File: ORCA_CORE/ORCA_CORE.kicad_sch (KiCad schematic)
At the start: 0 parts

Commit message: making usp
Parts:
- added J1: Conn_01x03, symbol Connector_Generic:Conn_01x03
- added J2: Conn_01x04, symbol Connector_Generic:Conn_01x04
- added J3, J5, J6, J7: Conn_01x02, symbol Connector_Generic:Conn_01x02
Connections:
- net power/Vout_usp: now also J7.2 (Pin_2)
- net power/emerg_detector: now also J1.1 (Pin_1)
- net power/emerge_order: now also J1.3 (Pin_3)
- new net GND: J2.2 (Pin_2), J3.1 (Pin_1), J5.1 (Pin_1), J6.1 (Pin_1), J7.1 (Pin_1)
- new net power/5V_I2C: J2.1 (Pin_1)
- new net power/SCL_3V3: J2.3 (Pin_3)
- new net power/SDA_3V3: J2.4 (Pin_4)
- new net power/Vin_bat: J5.2 (Pin_2)
- new net power/Vin_ex: J6.2 (Pin_2)
- new net power/Vout_motor: J3.2 (Pin_2)
- new net power/power_checker: J1.2 (Pin_2)
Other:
- sheet power ports: added 5V_I2C, GND, SCL_3V3, SDA_3V3, Vin_bat, Vin_ex, Vout_motor, power_checker; removed GND_out, Vout_cpu, battery_checker

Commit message: made usp (sketch only)
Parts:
- added J8: Vin_power2usp, symbol Connector_Generic:Conn_01x02
- added J9: +5Vout_cpu, symbol Connector_Generic:Conn_01x02
- J1: value Conn_01x03 -> data_line_power
- J2: value Conn_01x04 -> I2C_power
- J3: value Conn_01x02 -> Vout_motor
- J5: value Conn_01x02 -> Vin_batt
- J6: value Conn_01x02 -> Vin_ex
- J7: value Conn_01x02 -> Vout_power2usp
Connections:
- net GND: now also J8.1 (Pin_1), J9.1 (Pin_1)
- net power/5V_I2C renamed power/3V_I2C
- new net usp/Vin: J8.2 (Pin_2)
- new net usp/Vout: J9.2 (Pin_2)
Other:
- sheet power ports: added 3V_I2C; removed 5V_I2C
- sheet usp ports: added GND, Vin, Vout; removed none
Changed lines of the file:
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@@
+    (stroke (width 0) (type default))
+  )
+  (wire (pts (xy 58.42 100.33) (xy 67.31 100.33))
     (stroke (width 0) (type default))
   )
@@
     (stroke (width 0) (type default))
   )
+  (wire (pts (xy 66.04 93.98) (xy 66.04 86.36))
+    (stroke (width 0) (type default))
+  )
+  (wire (pts (xy 58.42 93.98) (xy 66.04 93.98))
+    (stroke (width 0) (type default))
+  )
   (wire (pts (xy 71.12 53.34) (xy 80.01 53.34))
     (stroke (width 0) (type default))
@@
     (stroke (width 0) (type default))
   )
+  (symbol (lib_id "power:GND") (at 67.31 97.79 270) (unit 1)
+    (in_bom yes) (on_board yes) (dnp no) (fields_autoplaced)
+    (property "Reference" "#PWR069" (at 60.96 97.79 0)
+      (effects (font (size 1.27 1.27)) hide)
+    )
+    (property "Value" "GND" (at 63.5 97.79 90)
+      (effects (font (size 1.27 1.27)) (justify right))
+    )
+    (property "Footprint" "" (at 67.31 97.79 0)
+      (effects (font (size 1.27 1.27)) hide)
+    )
+    (property "Datasheet" "" (at 67.31 97.79 0)
+      (effects (font (size 1.27 1.27)) hide)
+    )
+    (pin "1")
+    (instances
+      (project "ORCA_CORE"
+        (path "/895d6bb7-4008-488b-a34b-0077e9f7e4a1"
+          (reference "#PWR069") (unit 1)
+        )
+      )
+    )
+  )
+  (symbol (lib_id "power:GND") (at 58.42 105.41 90) (unit 1)
+    (in_bom yes) (on_board yes) (dnp no) (fields_autoplaced)
+    (property "Reference" "#PWR070" (at 64.77 105.41 0)
+      (effects (font (size 1.27 1.27)) hide)
+    )
+    (property "Value" "GND" (at 62.23 105.41 90)
+      (effects (font (size 1.27 1.27)) (justify right))
+    )
+    (property "Footprint" "" (at 58.42 105.41 0)
+      (effects (font (size 1.27 1.27)) hide)
+    )
+    (property "Datasheet" "" (at 58.42 105.41 0)
+      (effects (font (size 1.27 1.27)) hide)
+    )
+    (pin "1")
+    (instances
+      (project "ORCA_CORE"
+        (path "/895d6bb7-4008-488b-a34b-0077e9f7e4a1"
+          (reference "#PWR070") (unit 1)
+        )
+      )
+    )
+  )
   (symbol (lib_id "power:GND") (at 27.94 29.21 90) (unit 1)
     (in_bom yes) (on_board yes) (dnp no) (fields_autoplaced)
@@
     )
   )
+  (symbol (lib_id "Connector_Generic:Conn_01x02") (at 72.39 97.79 0) (unit 1)
+    (in_bom yes) (on_board yes) (dnp no) (fields_autoplaced)
+    (property "Reference" "J9" (at 74.93 97.79 0)
+      (effects (font (size 1.27 1.27)) (justify left))
+    )
+    (property "Value" "+5Vout_cpu" (at 74.93 100.33 0)
+      (effects (font (size 1.27 1.27)) (justify left))
+    )
+    (property "Footprint" "" (at 72.39 97.79 0)
+      (effects (font (size 1.27 1.27)) hide)
+    )
+    (property "Datasheet" "~" (at 72.39 97.79 0)
+      (effects (font (size 1.27 1.27)) hide)
+    )
+    (pin "2")
+    (pin "1")
+    (instances
+      (project "ORCA_CORE"
+        (path "/895d6bb7-4008-488b-a34b-0077e9f7e4a1"
+          (reference "J9") (unit 1)
+        )
+      )
+    )
+  )
+  (symbol (lib_id "Connector_Generic:Conn_01x02") (at 63.5 81.28 90) (unit 1)
+    (in_bom yes) (on_board yes) (dnp no) (fields_autoplaced)
+    (property "Reference" "J8" (at 68.58 80.01 90)
+      (effects (font (size 1.27 1.27)) (justify right))
+    )
+    (property "Value" "Vin_power2usp" (at 68.58 82.55 90)
+      (effects (font (size 1.27 1.27)) (justify right))
+    )
+    (property "Footprint" "" (at 63.5 81.28 0)
+      (effects (font (size 1.27 1.27)) hide)
+    )
+    (property "Datasheet" "~" (at 63.5 81.28 0)
+      (effects (font (size 1.27 1.27)) hide)
+    )
+    (pin "2")
+    (pin "1")
+    (instances
+      (project "ORCA_CORE"
+        (path "/895d6bb7-4008-488b-a34b-0077e9f7e4a1"
+          (reference "J8") (unit 1)
+        )
+      )
+    )
+  )
   (symbol (lib_id "power:GND") (at 68.58 69.85 90) (unit 1)
     (in_bom yes) (on_board yes) (dnp no) (fields_autoplaced)
@@
       (effects (font (size 1.27 1.27)) (justify left))
     )
-    (property "Value" "Conn_01x04" (at 87.63 50.8 0)
+    (property "Value" "I2C_power" (at 87.63 50.8 0)
       (effects (font (size 1.27 1.27)) (justify left))
     )
@@
       (effects (font (size 1.27 1.27)) (justify left))
     )
-    (property "Value" "Conn_01x03" (at 87.63 38.1 0)
+    (property "Value" "data_line_power" (at 87.63 38.1 0)
       (effects (font (size 1.27 1.27)) (justify left))
     )
@@
     )
   )
+  (symbol (lib_id "power:GND") (at 63.5 86.36 0) (unit 1)
+    (in_bom yes) (on_board yes) (dnp no) (fields_autoplaced)
+    (property "Reference" "#PWR068" (at 63.5 92.71 0)
+      (effects (font (size 1.27 1.27)) hide)
+    )
+    (property "Value" "GND" (at 63.5 91.44 0)
+      (effects (font (size 1.27 1.27)))
+    )
+    (property "Footprint" "" (at 63.5 86.36 0)
+      (effects (font (size 1.27 1.27)) hide)
+    )
+    (property "Datasheet" "" (at 63.5 86.36 0)
+      (effects (font (size 1.27 1.27)) hide)
+    )
+    (pin "1")
+    (instances
+      (project "ORCA_CORE"
+        (path "/895d6bb7-4008-488b-a34b-0077e9f7e4a1"
+          (reference "#PWR068") (unit 1)
+        )
+      )
+    )
+  )
   (symbol (lib_id "power:GND") (at 27.94 43.18 90) (unit 1)
     (in_bom yes) (on_board yes) (dnp no) (fields_autoplaced)
@@
       (effects (font (size 1.27 1.27)) (justify left))
     )
-    (property "Value" "Conn_01x02" (at 68.58 77.47 90)
+    (property "Value" "Vout_power2usp" (at 68.58 77.47 90)
       (effects (font (size 1.27 1.27)) (justify left))
     )
@@
       (effects (font (size 1.27 1.27)))
     )
-    (property "Value" "Conn_01x02" (at 22.86 36.83 0)
+    (property "Value" "Vin_ex" (at 22.86 36.83 0)
       (effects (font (size 1.27 1.27)))
     )
@@
       (effects (font (size 1.27 1.27)))
     )
-    (property "Value" "Conn_01x02" (at 22.86 22.86 0)
+    (property "Value" "Vin_batt" (at 22.86 22.86 0)
       (effects (font (size 1.27 1.27)))
     )
@@
       (effects (font (size 1.27 1.27)) (justify left))
     )
-    (property "Value" "Conn_01x02" (at 87.63 26.67 0)
+    (property "Value" "Vout_motor" (at 87.63 26.67 0)
       (effects (font (size 1.27 1.27)) (justify left))
     )
@@
       (effects (font (size 1.27 1.27)) (justify right))
     )
-    (pin "5V_I2C" output (at 71.12 45.72 0)
-      (effects (font (size 1.27 1.27)) (justify right))
-    )
     (pin "GND" output (at 68.58 66.04 270)
       (effects (font (size 1.27 1.27)) (justify left))
     )
+    (pin "3V_I2C" output (at 71.12 45.72 0)
+      (effects (font (size 1.27 1.27)) (justify right))
+    )
     (instances
       (project "ORCA_CORE"
@@
     )
   )
-  (sheet (at 46.228 137.922) (size 32.131 24.765) (fields_autoplaced)
+  (sheet (at 45.72 90.932) (size 12.7 18.288) (fields_autoplaced)
     (stroke (width 0.1524) (type solid))
     (fill (color 255 255 255 0.0000))
-    (property "Sheetname" "usp" (at 46.228 137.2104 0)
+    (property "Sheetname" "usp" (at 45.72 90.2204 0)
       (effects (font (size 1.27 1.27)) (justify left bottom))
     )
-    (property "Sheetfile" "usp.kicad_sch" (at 46.228 163.2716 0)
+    (property "Sheetfile" "usp.kicad_sch" (at 45.72 109.8046 0)
       (effects (font (size 1.27 1.27)) (justify left top))
     )
+    (pin "GND" output (at 58.42 105.41 0)
+      (effects (font (size 1.27 1.27)) (justify right))
+    )
+    (pin "Vin" input (at 58.42 93.98 0)
+      (effects (font (size 1.27 1.27)) (justify right))
+    )
+    (pin "Vout" input (at 58.42 100.33 0)
+      (effects (font (size 1.27 1.27)) (justify right))
+    )
     (instances
       (project "ORCA_CORE"
@@
     )
   )
-  (sheet (at 107.188 57.277) (size 33.782 42.164) (fields_autoplaced)
+  (sheet (at 116.078 24.257) (size 33.782 42.164) (fields_autoplaced)
     (stroke (width 0.1524) (type solid))
     (fill (color 255 255 255 0.0000))
-    (property "Sheetname" "cpu" (at 107.188 56.5654 0)
+    (property "Sheetname" "cpu" (at 116.078 23.5454 0)
       (effects (font (size 1.27 1.27)) (justify left bottom))
     )
-    (property "Sheetfile" "cpu.kicad_sch" (at 107.188 100.0256 0)
+    (property "Sheetfile" "cpu.kicad_sch" (at 116.078 67.0056 0)
       (effects (font (size 1.27 1.27)) (justify left top))
     )
-    (property "フィールド2" "" (at 107.188 57.277 0)
-      (effects (font (size 1.27 1.27)) hide)
-    )
+    (property "フィールド2" "" (at 116.078 24.257 0)
+      (effects (font (size 1.27 1.27)) hide)
+    )

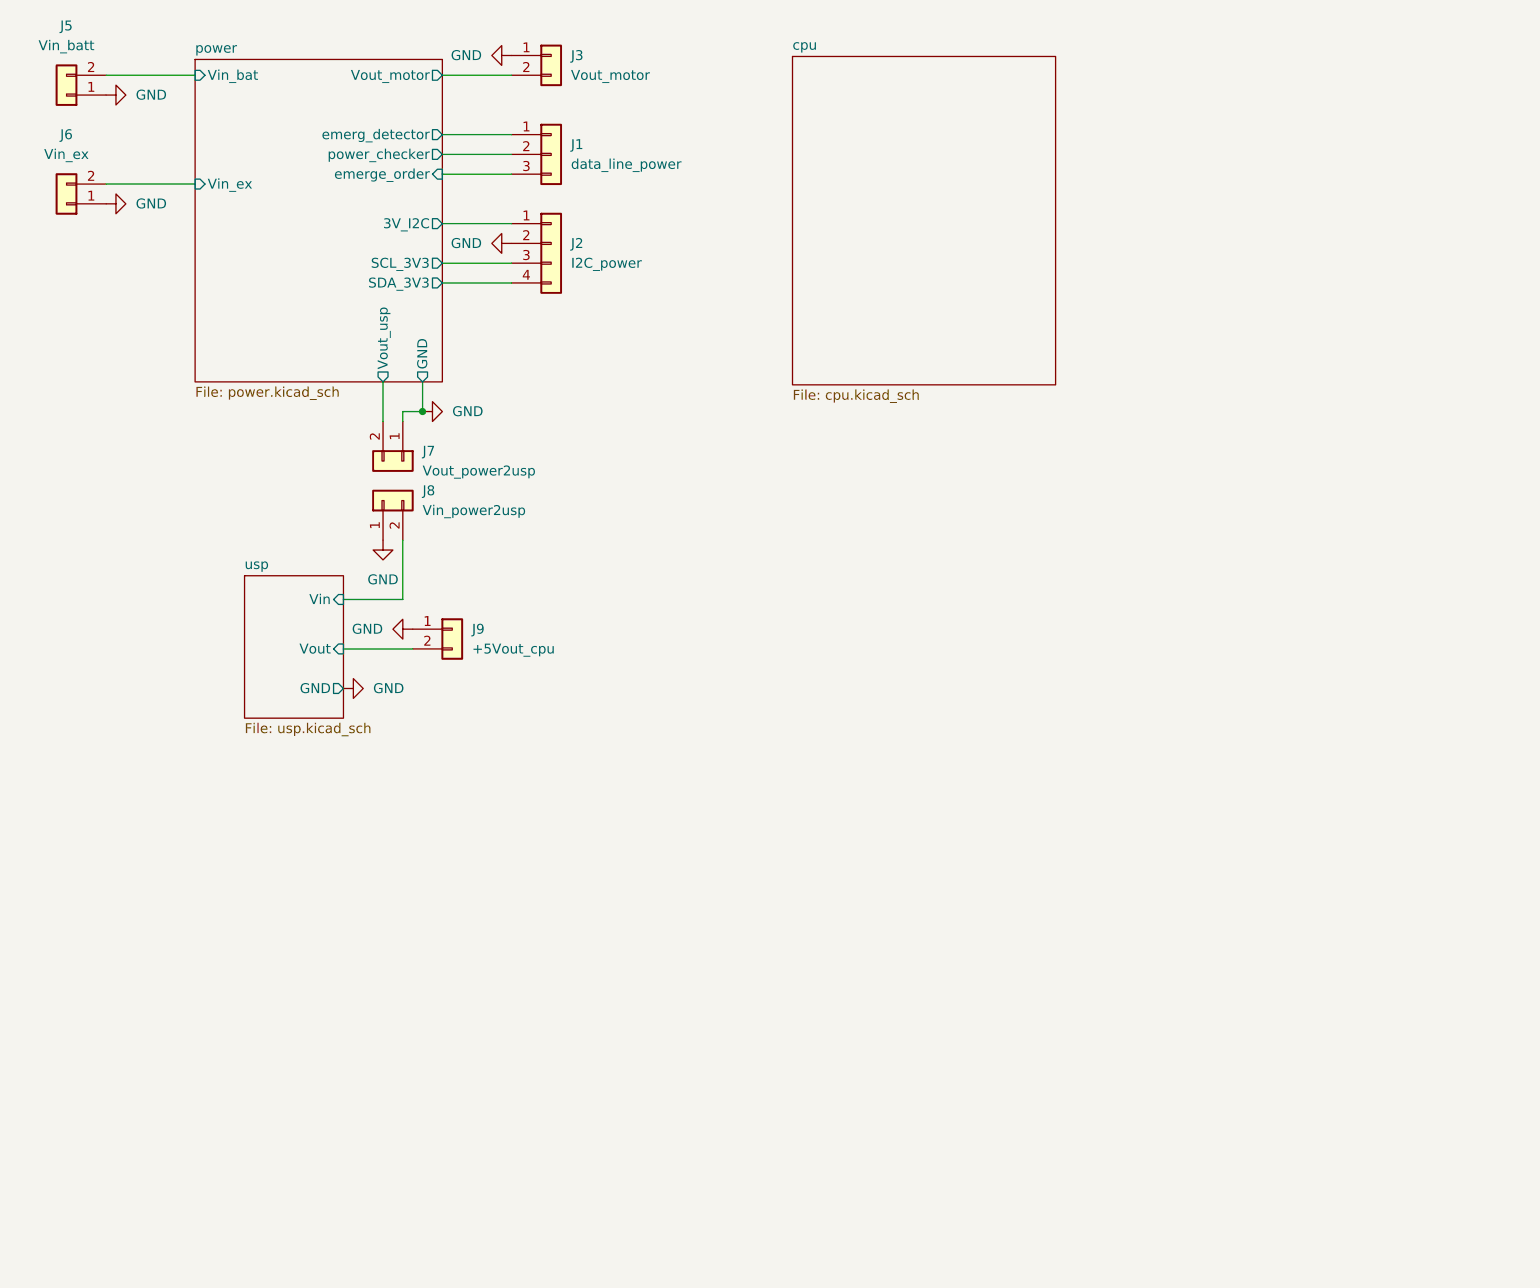
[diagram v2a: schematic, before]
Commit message: made all sketch for test (cpu board is only for test
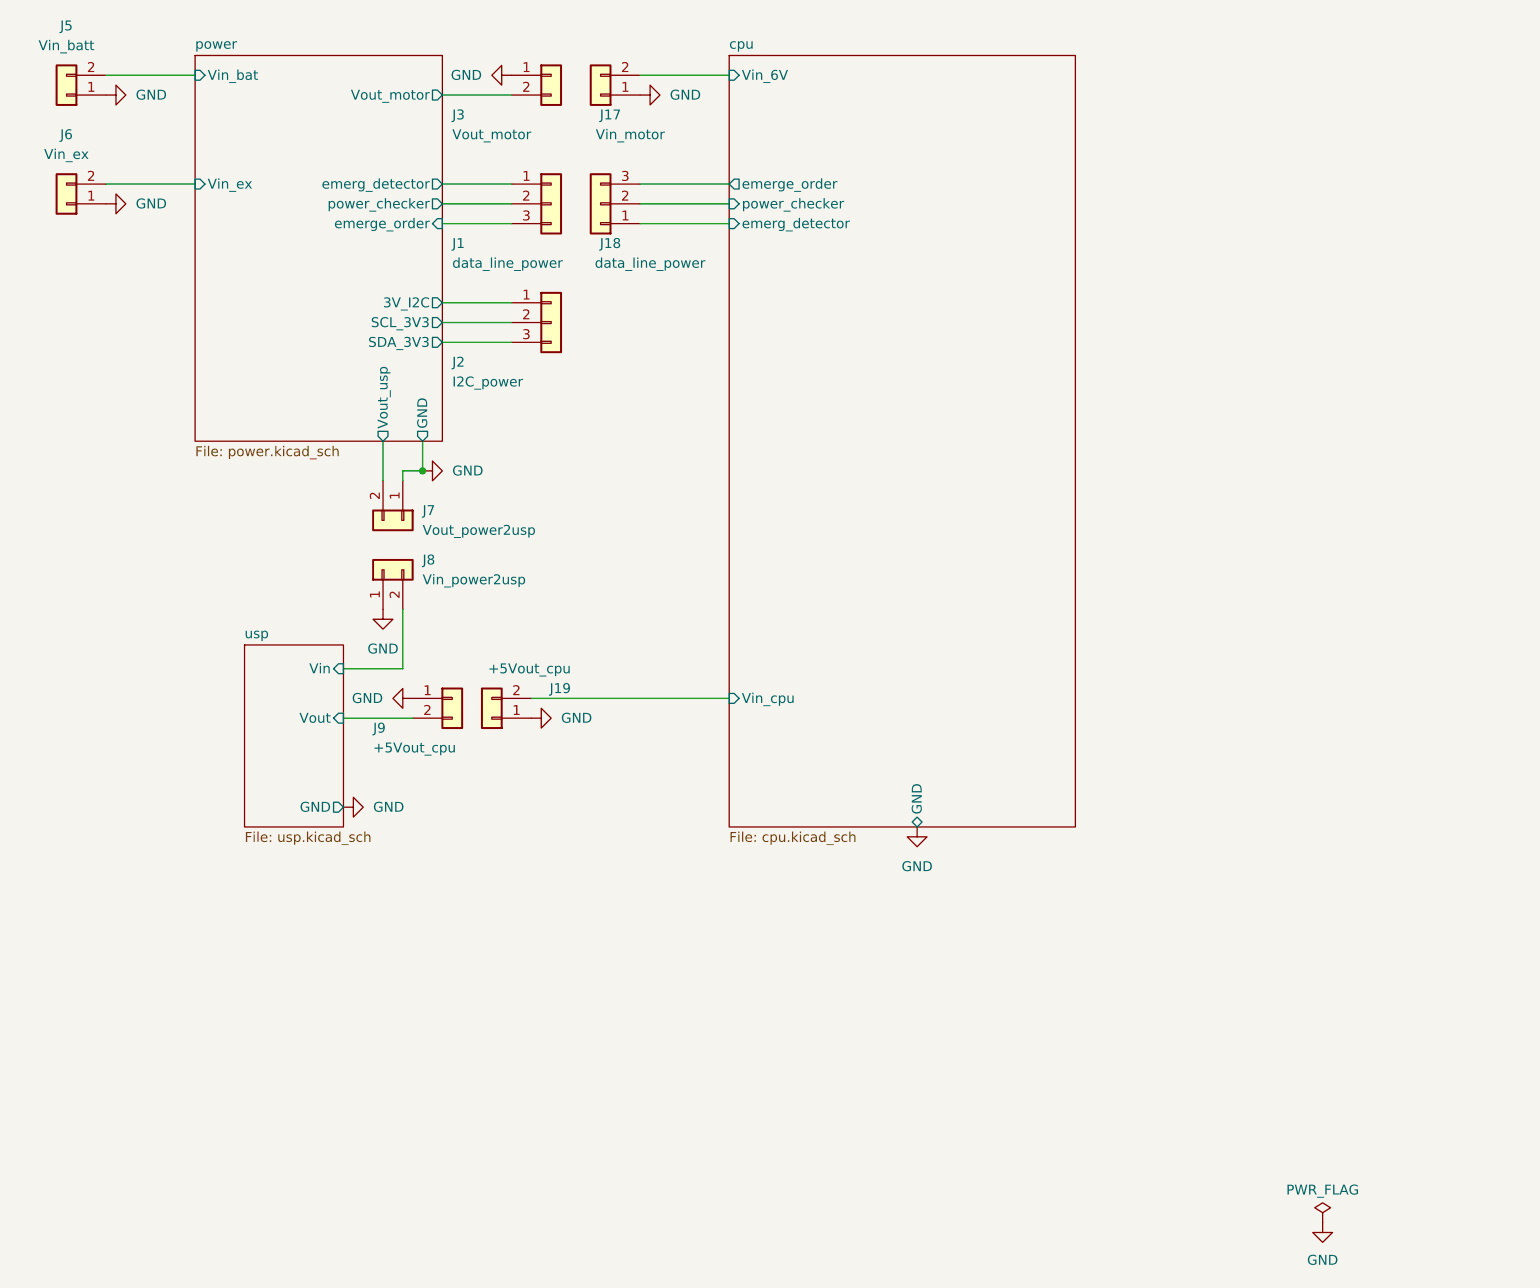
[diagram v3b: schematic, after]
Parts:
- removed J2: I2C_power, symbol Connector_Generic:Conn_01x04
- added J17: Vin_motor, symbol Connector_Generic:Conn_01x02
- added J18: data_line_power, symbol Connector_Generic:Conn_01x03
- added J19: +5Vout_cpu, symbol Connector_Generic:Conn_01x02
- added J2: I2C_power, symbol Connector_Generic:Conn_01x03
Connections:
- net GND: now also J17.1 (Pin_1), J19.1 (Pin_1)
- net power/3V_I2C: now also J2.1 (Pin_1)
- net power/SCL_3V3: now also J2.2 (Pin_2)
- net power/SDA_3V3: now also J2.3 (Pin_3)
- new net cpu/Vin_6V: J17.2 (Pin_2)
- new net cpu/Vin_cpu: J19.2 (Pin_2)
- new net cpu/emerg_detector: J18.1 (Pin_1)
- new net cpu/emerge_order: J18.3 (Pin_3)
- new net cpu/power_checker: J18.2 (Pin_2)
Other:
- sheet cpu ports: added GND, Vin_6V, Vin_cpu, emerg_detector, emerge_order, power_checker; removed none
- moved on the sheet: J1, J3, J7, J8, J9

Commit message: attach all the footprints
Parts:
- J1, J2: footprint (none) -> Connector_JST:JST_XH_B3B-XH-A_1x03_P2.50mm_Vertical
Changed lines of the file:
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@@
       (effects (font (size 1.27 1.27)) (justify left))
     )
-    (property "Footprint" "" (at 85.09 58.42 0)
+    (property "Footprint" "Connector_JST:JST_XH_B3B-XH-A_1x03_P2.50mm_Vertical" (at 85.09 58.42 0)
       (effects (font (size 1.27 1.27)) hide)
     )
@@
       (effects (font (size 1.27 1.27)) (justify left))
     )
-    (property "Footprint" "" (at 85.09 43.18 0)
+    (property "Footprint" "Connector_JST:JST_XH_B3B-XH-A_1x03_P2.50mm_Vertical" (at 85.09 43.18 0)
       (effects (font (size 1.27 1.27)) hide)
     )

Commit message: change sketch a little
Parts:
- J17, J19, J3, J5, J6, J7, J8, J9: footprint (none) -> Conn:power_pad
- J18: footprint (none) -> Connector_JST:JST_XH_B3B-XH-A_1x03_P2.50mm_Vertical
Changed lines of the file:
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@@
       (effects (font (size 1.27 1.27)) (justify left))
     )
-    (property "Footprint" "" (at 72.39 106.68 0)
+    (property "Footprint" "Conn:power_pad" (at 72.39 106.68 0)
       (effects (font (size 1.27 1.27)) hide)
     )
@@
       (effects (font (size 1.27 1.27)) (justify right))
     )
-    (property "Footprint" "" (at 63.5 90.17 0)
+    (property "Footprint" "Conn:power_pad" (at 63.5 90.17 0)
       (effects (font (size 1.27 1.27)) hide)
     )
@@
       (effects (font (size 1.27 1.27)))
     )
-    (property "Footprint" "" (at 91.44 29.21 0)
+    (property "Footprint" "Conn:power_pad" (at 91.44 29.21 0)
       (effects (font (size 1.27 1.27)) hide)
     )
@@
       (effects (font (size 1.27 1.27)) (justify left))
     )
-    (property "Footprint" "" (at 77.47 109.22 0)
+    (property "Footprint" "Conn:power_pad" (at 77.47 109.22 0)
       (effects (font (size 1.27 1.27)) hide)
     )
@@
       (effects (font (size 1.27 1.27)) (justify left))
     )
-    (property "Footprint" "" (at 66.04 83.82 0)
+    (property "Footprint" "Conn:power_pad" (at 66.04 83.82 0)
       (effects (font (size 1.27 1.27)) hide)
     )
@@
       (effects (font (size 1.27 1.27)))
     )
-    (property "Footprint" "" (at 22.86 43.18 0)
+    (property "Footprint" "Conn:power_pad" (at 22.86 43.18 0)
       (effects (font (size 1.27 1.27)) hide)
     )
@@
       (effects (font (size 1.27 1.27)))
     )
-    (property "Footprint" "" (at 22.86 29.21 0)
+    (property "Footprint" "Conn:power_pad" (at 22.86 29.21 0)
       (effects (font (size 1.27 1.27)) hide)
     )
@@
       (effects (font (size 1.27 1.27)))
     )
-    (property "Footprint" "" (at 91.44 43.18 0)
+    (property "Footprint" "Connector_JST:JST_XH_B3B-XH-A_1x03_P2.50mm_Vertical" (at 91.44 43.18 0)
       (effects (font (size 1.27 1.27)) hide)
     )
@@
       (effects (font (size 1.27 1.27)) (justify left))
     )
-    (property "Footprint" "" (at 85.09 26.67 0)
-      (effects (font (size 1.27 1.27)) hide)
-    )
+    (property "Footprint" "Conn:power_pad" (at 85.09 26.67 0)
+      (effects (font (size 1.27 1.27)) hide)
+    )
